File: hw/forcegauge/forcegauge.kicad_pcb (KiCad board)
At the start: 2 copper layers, 60 x 40 mm, 73 parts, among them J1 USB_B_Micro, J2 Battery, J3 OLDED_Screen, J4 Load Cell, Q1 FDS6892A, Q2 BSS138, Q3 SM2331PSA P-MOSFET, Q4 S8550, Q5 FDS6892A, SW1 SW_Push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

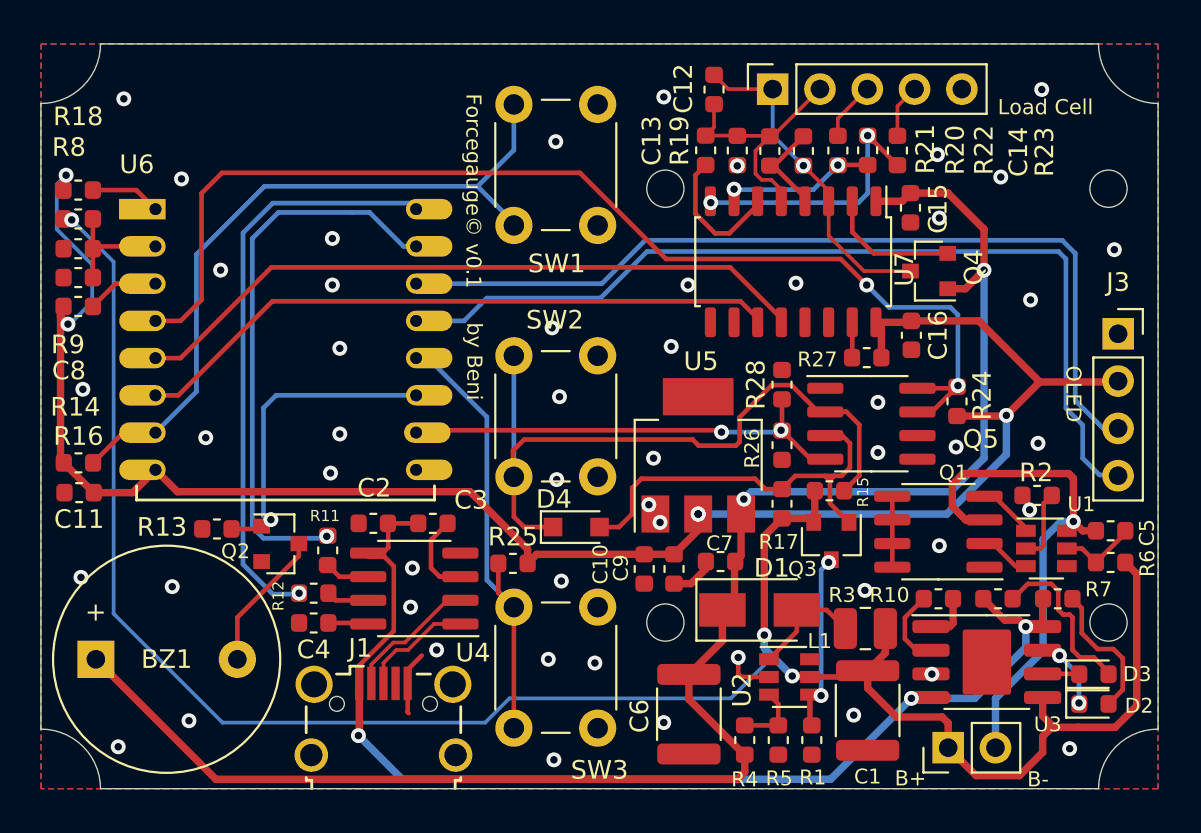
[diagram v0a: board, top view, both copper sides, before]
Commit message: button dir updated, fixed footprints and changed dual fet
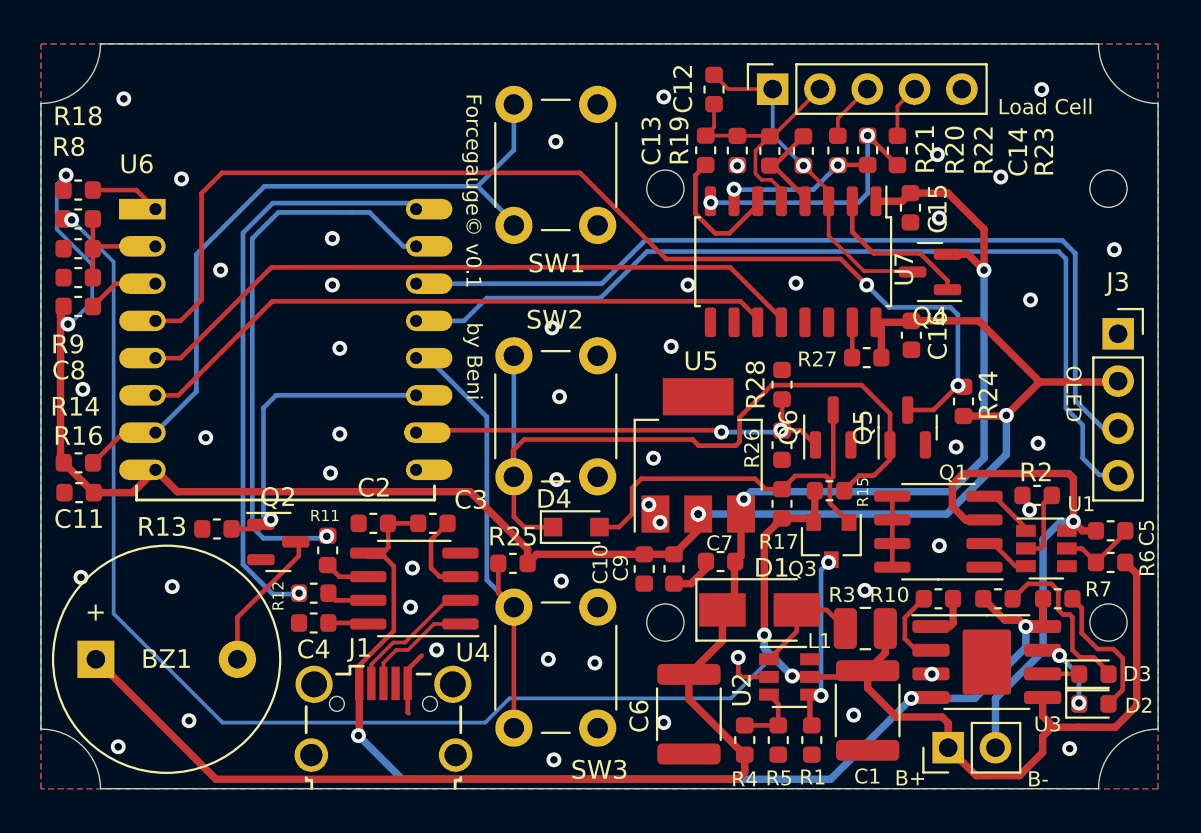
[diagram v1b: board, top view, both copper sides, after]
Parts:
- added Q6: BSS138, Package_TO_SOT_SMD:SOT-23, F.Cu at (163.4, 101.8)
- Q5: value FDS6892A -> BSS138; footprint Package_SO:SOIC-8_3.9x4.9mm_P1.27mm -> Package_TO_SOT_SMD:SOT-23
- moved Q5 1.96 mm to (167.4, 101.8), turned to 90 degrees
- moved R24 0.35 mm to (170.4, 100.4)
- moved Q2 0.14 mm to (133.6, 108.0)
- moved Q4 0.07 mm to (168.6, 93.5)
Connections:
- Q4 pad 1: +5V -> Net-(Q4-Pad1)
- Q4 pad 2: Net-(Q4-Pad2) -> +5V
- Q5 pad 1: GND -> Net-(D4-Pad1)
- Q5 pad 2: Net-(D4-Pad1) -> GND
- Q5 pad 3: Net-(D4-Pad2) -> BTN_2
- U7 pad 2: Net-(Q4-Pad2) -> Net-(Q4-Pad1)
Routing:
- net Net-(Q4-Pad1): track 0.00 -> 8.33 mm
- net Net-(Q4-Pad2): track 7.25 -> 0.00 mm
- net Net-(D4-Pad1): track 38.3 -> 41.4 mm
- net BTN_2: track 61.5 -> 60.1 mm
- net PWR_EN: track 24.6 -> 23.7 mm
- net Net-(D4-Pad2): track 22.3 -> 21.4 mm
- net GND: vias 51 -> 49

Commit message: pcb v0.2 fixed errors
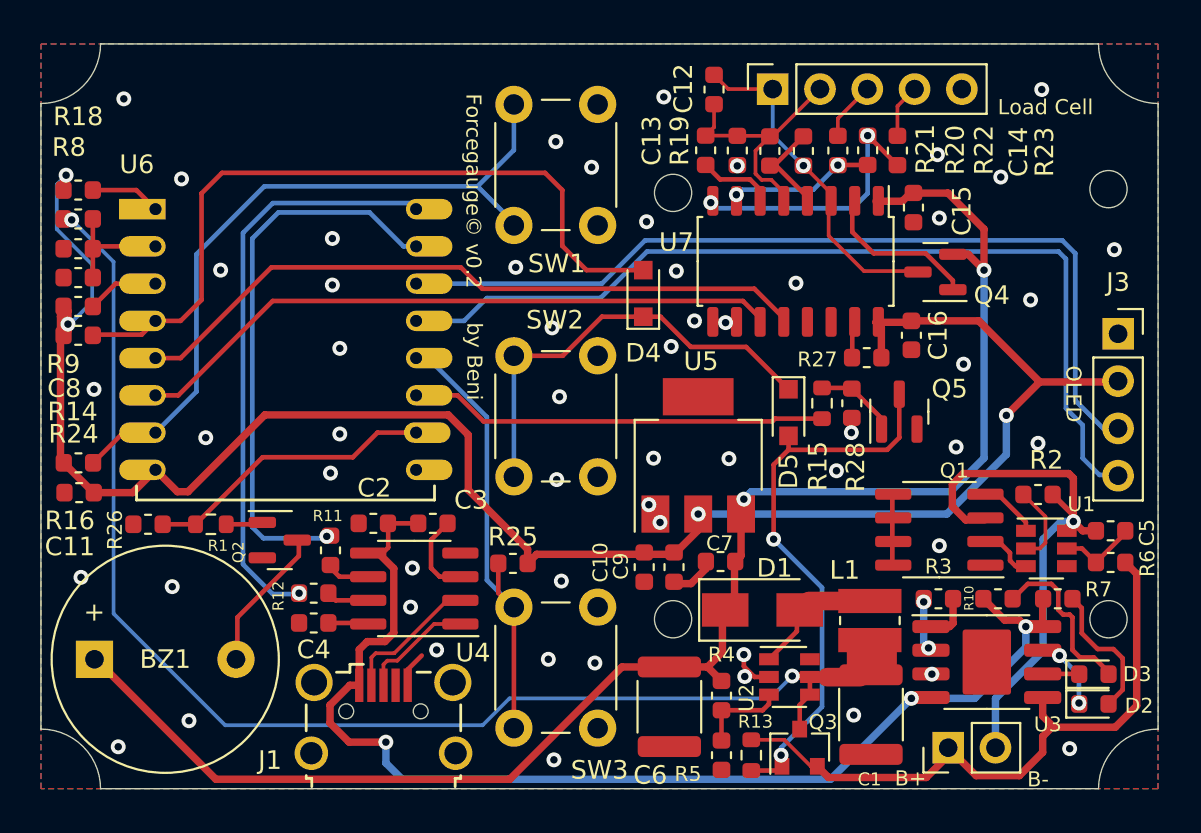
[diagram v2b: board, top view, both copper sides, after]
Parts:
- removed Q6: BSS138, Package_TO_SOT_SMD:SOT-23
- removed R17: 100k, Resistor_SMD:R_0603_1608Metric
- added D5: 1SS355, Diode_SMD:D_SOD-323_HandSoldering, F.Cu at (161.0, 101.0)
- L1: footprint Inductor_SMD:L_1008_2520Metric -> Inductor_SMD:L_Wuerth_MAPI-3012
- R1, R15: value 100k -> 100
- moved R24 47.7 mm to (122.8, 96.9), turned to 180 degrees
- moved R26 34.3 mm to (126.6, 107.0), turned to 0 degrees
- moved R1 34.3 mm to (130.0, 107.0), turned to 180 degrees
- moved R13 31.2 mm to (159.0, 119.5), turned to 90 degrees
- moved D4 13.1 mm to (153.2, 94.7), turned to 90 degrees
- moved Q3 11.2 mm to (161.6, 119.0), turned to 90 degrees
- moved R15 4.72 mm to (162.8, 100.5), turned to 90 degrees
- moved R28 3.88 mm to (164.4, 100.5), turned to 90 degrees
- moved R5 3.16 mm to (157.4, 119.5)
- moved R4 2.69 mm to (157.4, 116.2), turned to 90 degrees
- moved C6 1.12 mm to (154.6, 116.8)
- moved Q5 0.96 mm to (166.9, 101.0)
- moved L1 0.49 mm to (165.4, 112.2), turned to 90 degrees
- moved H2 0.47 mm to (154.8, 89.2)
- moved H3 0.45 mm to (154.8, 112.2)
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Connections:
- C1 pad 1: BAT+ -> VCC
- D4 pad 2: Net-(D4-Pad2) -> BTN_2
- L1 pad 1: BAT+ -> VCC
- Q2 pad 1: BUZZER -> Net-(Q2-Pad1)
- Q3 pad 1: Net-(D4-Pad2) -> Net-(Q3-Pad1)
- Q3 pad 3: 5V_EN -> VCC
- Q5 pad 1: Net-(D4-Pad1) -> Net-(R15-Pad2)
- Q5 pad 3: BTN_2 -> Net-(Q3-Pad1)
- R1 pad 1: GND -> Net-(Q2-Pad1)
- R1 pad 2: 5V_EN -> BUZZER
- R13 pad 1: GND -> Net-(Q3-Pad1)
- R13 pad 2: BUZZER -> BAT+
- R15 pad 1: Net-(D4-Pad1) -> PWR_EN
- R15 pad 2: BAT+ -> Net-(R15-Pad2)
- R2 pad 2: GND -> BAT-
- R26 pad 2: PWR_EN -> BUZZER
- R28 pad 2: PWR_EN -> Net-(R15-Pad2)
- R8 pad 1: BAT+ -> VCC
- U2 pad 4: 5V_EN -> VCC
- U2 pad 5: BAT+ -> VCC
- U6 pad 10: PWR_EN -> BUZZER
- U6 pad 11: BUZZER -> PWR_EN
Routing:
- net BAT+: track 113.5 -> 34.9 mm, vias 3 -> 0
- net VCC: track 0.00 -> 76.5 mm, vias 0 -> 2
- net Net-(Q3-Pad1): track 0.00 -> 30.4 mm, vias 0 -> 2
- net Net-(D4-Pad2): track 21.4 -> 0.00 mm
- net BTN_2: track 60.1 -> 40.5 mm, vias 2 -> 0
- net Net-(D4-Pad1): track 41.4 -> 23.7 mm
- net 5V_EN: track 9.96 -> 0.00 mm, vias 2 -> 0
- net +5V: track 90.1 -> 85.7 mm
- net Net-(R15-Pad2): track 0.00 -> 4.45 mm
- net +3V3: track 101.1 -> 105.4 mm, vias 5 -> 4
- net Net-(C13-Pad1): track 7.46 -> 3.47 mm
- net VBUS: track 64.0 -> 66.1 mm
- net Net-(D1-Pad2): track 6.29 -> 8.20 mm
- net BAT-: track 28.7 -> 30.6 mm
- net Net-(Q2-Pad1): track 0.00 -> 1.86 mm
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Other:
- board text added: "Forcegauge© v0.2"
- board text removed: "Forcegauge© v0.1"

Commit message: pcb and box updata
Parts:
- added H5: PCB Mounting hole, forcegauge:MountingHole_2mm_OLED, F.Cu at (122.3, 119.8)
- added H6: PCB Mounting hole, forcegauge:MountingHole_2mm_OLED, F.Cu at (179.4, 119.8)
- added H7: PCB Mounting hole, forcegauge:MountingHole_2mm_OLED, F.Cu at (122.3, 82.6)
- added H8: PCB Mounting hole, forcegauge:MountingHole_2mm_OLED, F.Cu at (179.4, 82.6)
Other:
- outline, holes or cut-outs redrawn
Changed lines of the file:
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@@
   (net 54 "Net-(Q4-Pad1)")
   (net 55 "VCC")
-  (net 56 "Net-(Q3-Pad1)")
+  (net 56 "Net-(D5-Pad2)")
   (net 57 "Net-(Q2-Pad1)")
-  (net 58 "Net-(R15-Pad2)")
+  (net 58 "Net-(Q5-Pad1)")
   (footprint "Buzzer_Beeper:Buzzer_12x9.5RM7.6" (layer "F.Cu")
     (at 123.725 114.299999)
@@
     (fp_line (start -0.7 -0.95) (end -0.15 -1.52) (layer "F.Fab") (width 0.1))
     (pad "1" smd rect locked (at -1 -0.95 90) (size 0.9 0.8) (layers "F.Cu" "F.Paste" "F.Mask")
-      (net 56 "Net-(Q3-Pad1)") (pinfunction "G") (pintype "input"))
+      (net 56 "Net-(D5-Pad2)") (pinfunction "G") (pintype "input"))
     (pad "2" smd rect locked (at -1 0.95 90) (size 0.9 0.8) (layers "F.Cu" "F.Paste" "F.Mask")
       (net 4 "BAT+") (pinfunction "S") (pintype "passive"))
@@
       (net 3 "GND") (pintype "passive"))
     (pad "2" smd roundrect locked (at 0.7875 0 90) (size 0.875 0.95) (layers "F.Cu" "F.Paste" "F.Mask") (roundrect_rratio 0.25)
-      (net 58 "Net-(R15-Pad2)") (pintype "passive"))
+      (net 58 "Net-(Q5-Pad1)") (pintype "passive"))
     (model "${KISYS3DMOD}/Resistor_SMD.3dshapes/R_0603_1608Metric.wrl"
       (offset (xyz 0 0 0))
@@
   )
   (footprint "forcegauge:MountingHole_2mm_OLED" (layer "F.Cu")
+    (at 179.4 119.825)
+    (descr "Mounting Hole 2mm, no annular")
+    (tags "mounting hole 2mm no annular")
+    (property "Sheetfile" "forcegauge.kicad_sch")
+    (property "Sheetname" "")
+    (attr exclude_from_pos_files)
+    (fp_text reference "H6" (at 1.15 -1.41) (layer "F.SilkS") hide
+      (effects (font (size 1 1) (thickness 0.15)))
+    )
+    (fp_text value "PCB Mounting hole" (at 0 3.1) (layer "F.Fab")
+      (effects (font (size 1 1) (thickness 0.15)))
+    )
+    (fp_text user "${REFERENCE}" (at 0.3 0) (layer "F.Fab")
+      (effects (font (size 1 1) (thickness 0.15)))
+    )
+    (fp_circle (center 0 0) (end 1.1 0) (layer "Cmts.User") (width 0.15) (fill none))
+    (fp_circle (center 0 0) (end 1.1 0) (layer "F.CrtYd") (width 0.05) (fill none))
+    (pad "" np_thru_hole circle (at 0 0) (size 2 2) (drill 2) (layers *.Cu *.Mask))
+  )
+  (footprint "forcegauge:MountingHole_2mm_OLED" (layer "F.Cu")
     (at 178.186 89.05)
     (descr "Mounting Hole 2mm, no annular")
@@
     )
     (fp_text value "MountingHole" (at 0 3.1) (layer "F.Fab")
+      (effects (font (size 1 1) (thickness 0.15)))
+    )
+    (fp_text user "${REFERENCE}" (at 0.3 0) (layer "F.Fab")
+      (effects (font (size 1 1) (thickness 0.15)))
+    )
+    (fp_circle (center 0 0) (end 1.1 0) (layer "Cmts.User") (width 0.15) (fill none))
+    (fp_circle (center 0 0) (end 1.1 0) (layer "F.CrtYd") (width 0.05) (fill none))
+    (pad "" np_thru_hole circle (at 0 0) (size 2 2) (drill 2) (layers *.Cu *.Mask))
+  )
+  (footprint "forcegauge:MountingHole_2mm_OLED" (layer "F.Cu")
+    (at 179.4 82.625)
+    (descr "Mounting Hole 2mm, no annular")
+    (tags "mounting hole 2mm no annular")
+    (property "Sheetfile" "forcegauge.kicad_sch")
+    (property "Sheetname" "")
+    (attr exclude_from_pos_files)
+    (fp_text reference "H8" (at 0 -3.2) (layer "F.SilkS") hide
+      (effects (font (size 1 1) (thickness 0.15)))
+    )
+    (fp_text value "PCB Mounting hole" (at 0 3.1) (layer "F.Fab")
       (effects (font (size 1 1) (thickness 0.15)))
     )
@@
       (net 21 "Net-(D4-Pad1)") (pinfunction "K") (pintype "passive"))
     (pad "2" smd rect (at 1.25 0 270) (size 1 1) (layers "F.Cu" "F.Paste" "F.Mask")
-      (net 56 "Net-(Q3-Pad1)") (pinfunction "A") (pintype "passive"))
+      (net 56 "Net-(D5-Pad2)") (pinfunction "A") (pintype "passive"))
     (model "${KICAD6_3DMODEL_DIR}/Diode_SMD.3dshapes/D_SOD-323.wrl"
       (offset (xyz 0 0 0))
@@
       (rotate (xyz 0 0 0))
     )
+  )
+  (footprint "forcegauge:MountingHole_2mm_OLED" (layer "F.Cu")
+    (at 122.275 119.825)
+    (descr "Mounting Hole 2mm, no annular")
+    (tags "mounting hole 2mm no annular")
+    (property "Sheetfile" "forcegauge.kicad_sch")
+    (property "Sheetname" "")
+    (attr exclude_from_pos_files)
+    (fp_text reference "H5" (at 0 -3.2) (layer "F.SilkS") hide
+      (effects (font (size 1 1) (thickness 0.15)))
+    )
+    (fp_text value "PCB Mounting hole" (at 0 3.1) (layer "F.Fab")
+      (effects (font (size 1 1) (thickness 0.15)))
+    )
+    (fp_text user "${REFERENCE}" (at 0.3 0) (layer "F.Fab")
+      (effects (font (size 1 1) (thickness 0.15)))
+    )
+    (fp_circle (center 0 0) (end 1.1 0) (layer "Cmts.User") (width 0.15) (fill none))
+    (fp_circle (center 0 0) (end 1.1 0) (layer "F.CrtYd") (width 0.05) (fill none))
+    (pad "" np_thru_hole circle (at 0 0) (size 2 2) (drill 2) (layers *.Cu *.Mask))
   )
   (footprint "Capacitor_SMD:C_0603_1608Metric" (layer "F.Cu")
@@
   )
   (footprint "forcegauge:MountingHole_2mm_OLED" (layer "F.Cu")
+    (at 122.275 82.625)
+    (descr "Mounting Hole 2mm, no annular")
+    (tags "mounting hole 2mm no annular")
+    (property "Sheetfile" "forcegauge.kicad_sch")
+    (property "Sheetname" "")
+    (attr exclude_from_pos_files)
+    (fp_text reference "H7" (at 0 -3.2) (layer "F.SilkS") hide
+      (effects (font (size 1 1) (thickness 0.15)))
+    )
+    (fp_text value "PCB Mounting hole" (at 0 3.1) (layer "F.Fab")
+      (effects (font (size 1 1) (thickness 0.15)))
+    )
+    (fp_text user "${REFERENCE}" (at 0.3 0) (layer "F.Fab")
+      (effects (font (size 1 1) (thickness 0.15)))
+    )
+    (fp_circle (center 0 0) (end 1.1 0) (layer "Cmts.User") (width 0.15) (fill none))
+    (fp_circle (center 0 0) (end 1.1 0) (layer "F.CrtYd") (width 0.05) (fill none))
+    (pad "" np_thru_hole circle (at 0 0) (size 2 2) (drill 2) (layers *.Cu *.Mask))
+  )
+  (footprint "forcegauge:MountingHole_2mm_OLED" (layer "F.Cu")
     (at 154.8 89.25)
     (descr "Mounting Hole 2mm, no annular")
@@
     (fp_line (start 0.8 -0.4125) (end 0.8 0.4125) (layer "F.Fab") (width 0.1))
     (pad "1" smd roundrect (at -0.825 0 90) (size 0.8 0.95) (layers "F.Cu" "F.Paste" "F.Mask") (roundrect_rratio 0.25)
-      (net 56 "Net-(Q3-Pad1)") (pintype "passive"))
+      (net 56 "Net-(D5-Pad2)") (pintype "passive"))
     (pad "2" smd roundrect (at 0.825 0 90) (size 0.8 0.95) (layers "F.Cu" "F.Paste" "F.Mask") (roundrect_rratio 0.25)
       (net 4 "BAT+") (pintype "passive"))
@@
     (fp_line (start -0.325 -1.45) (end 0.65 -1.45) (layer "F.Fab") (width 0.1))
     (pad "1" smd roundrect (at -0.9375 -0.95 90) (size 1.475 0.6) (layers "F.Cu" "F.Paste" "F.Mask") (roundrect_rratio 0.25)
-      (net 58 "Net-(R15-Pad2)") (pinfunction "G") (pintype "input"))
+      (net 58 "Net-(Q5-Pad1)") (pinfunction "G") (pintype "input"))
     (pad "2" smd roundrect (at -0.9375 0.95 90) (size 1.475 0.6) (layers "F.Cu" "F.Paste" "F.Mask") (roundrect_rratio 0.25)
       (net 3 "GND") (pinfunction "S") (pintype "passive"))
     (pad "3" smd roundrect (at 0.9375 0 90) (size 1.475 0.6) (layers "F.Cu" "F.Paste" "F.Mask") (roundrect_rratio 0.25)
-      (net 56 "Net-(Q3-Pad1)") (pinfunction "D") (pintype "passive"))
+      (net 56 "Net-(D5-Pad2)") (pinfunction "D") (pintype "passive"))
     (model "${KICAD6_3DMODEL_DIR}/Package_TO_SOT_SMD.3dshapes/SOT-23.wrl"
       (offset (xyz 0 0 0))
@@
       (net 34 "PWR_EN") (pintype "passive"))
     (pad "2" smd roundrect (at 0.825 0 90) (size 0.8 0.95) (layers "F.Cu" "F.Paste" "F.Mask") (roundrect_rratio 0.25)
-      (net 58 "Net-(R15-Pad2)") (pintype "passive"))
+      (net 58 "Net-(Q5-Pad1)") (pintype "passive"))
     (model "${KICAD6_3DMODEL_DIR}/Resistor_SMD.3dshapes/R_0603_1608Metric.wrl"
       (offset (xyz 0 0 0))
@@
     )
   )
-  (gr_arc (start 120.85 118.049999) (mid 123.112742 118.987257) (end 124.05 121.249999) (layer "Edge.Cuts") (width 0.05))
-  (gr_line (start 124.05 121.249999) (end 177.65 121.249999) (layer "Edge.Cuts") (width 0.05))
-  (gr_line (start 177.65 81.249999) (end 124.05 81.249999) (layer "Edge.Cuts") (width 0.05))
-  (gr_line (start 180.85 118.049999) (end 180.85 84.449999) (layer "Edge.Cuts") (width 0.05))
-  (gr_arc (start 180.85 84.449999) (mid 178.587258 83.512741) (end 177.65 81.249999) (layer "Edge.Cuts") (width 0.05))
-  (gr_line (start 120.85 84.449999) (end 120.85 118.049999) (layer "Edge.Cuts") (width 0.05))
-  (gr_arc (start 124.05 81.249999) (mid 123.112742 83.512741) (end 120.85 84.449999) (layer "Edge.Cuts") (width 0.05))
-  (gr_arc (start 177.65 121.249999) (mid 178.587258 118.987257) (end 180.85 118.049999) (layer "Edge.Cuts") (width 0.05))
+  (gr_line (start 120.85 121.25) (end 180.85 121.25) (layer "Edge.Cuts") (width 0.05))
+  (gr_line (start 180.85 81.25) (end 120.85 81.25) (layer "Edge.Cuts") (width 0.05))
+  (gr_line (start 180.85 121.25) (end 180.85 81.25) (layer "Edge.Cuts") (width 0.05))
+  (gr_line (start 120.85 81.25) (end 120.85 121.25) (layer "Edge.Cuts") (width 0.05))
   (gr_text "B+" (at 167.55 120.7) (layer "F.SilkS")
     (effects (font (size 0.8128 0.8128) (thickness 0.1524)))

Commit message: v0.3 pcb
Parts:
- moved R16 24.2 mm to (145.3, 94.5), turned to 180 degrees
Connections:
- U6 pad 11: PWR_EN -> BTN_1
- U6 pad 5: DOUT -> CLK
- U6 pad 6: CLK -> DOUT
- U6 pad 7: BTN_1 -> PWR_EN
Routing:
- net BTN_1: track 39.3 -> 18.9 mm
- net PWR_EN: track 22.4 -> 38.0 mm, vias 0 -> 2
- net +3V3: track 105.4 -> 113.8 mm
- net CLK: track 35.4 -> 42.5 mm
- net BTN_3: track 25.2 -> 27.5 mm, vias 0 -> 1
- net DOUT: track 37.3 -> 38.1 mm, vias 0 -> 2
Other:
- board text added: "Forcegauge© v0.3"
- board text removed: "Forcegauge© v0.2"

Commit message: pcb v0.4
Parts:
- R28: value 100k -> 10k
- moved J3 0.61 mm to (178.7, 97.4)
- moved C5 0.47 mm to (178.3, 107.9)
- moved R6 0.36 mm to (178.3, 109.5)
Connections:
- C2 pad 1: VBUS -> +3V3
- C3 pad 1: VBUS -> +3V3
- U4 pad 5: VBUS -> +3V3
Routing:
- net VBUS: track 66.1 -> 52.7 mm
- net +3V3: track 113.8 -> 121.1 mm
- net BTN_3: track 27.5 -> 29.4 mm
- net SCL: track 47.5 -> 48.5 mm
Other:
- board text added: "Forcegauge© v0.4"
- board text removed: "Forcegauge© v0.3"
